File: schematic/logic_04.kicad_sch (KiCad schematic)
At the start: 4 parts, among them U418 74HC08, U421 74HC08, U423 74HC08, U425 74HC08

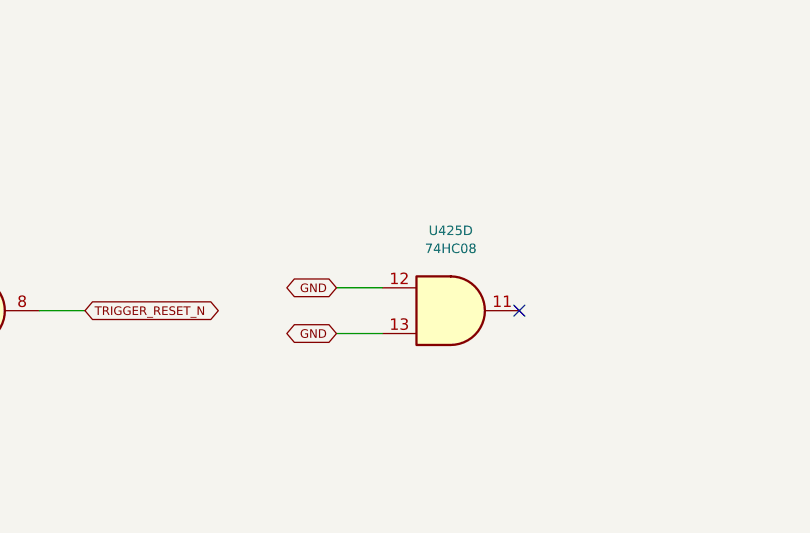
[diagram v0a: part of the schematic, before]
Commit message: add power supply, rail checks and parts list
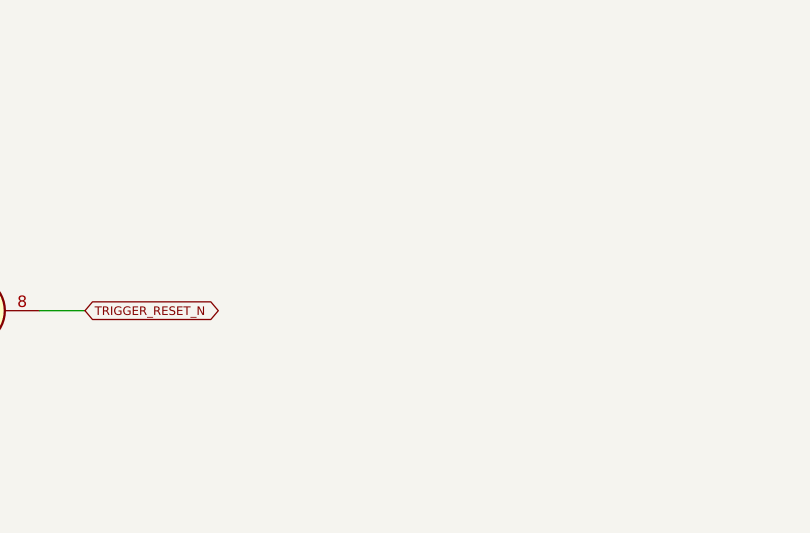
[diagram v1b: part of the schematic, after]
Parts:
- removed unit 4 of U425
- U418, U421, U423, U425: MPN (none) -> 74HC08D,653; Manufacturer (none) -> Nexperia; Supplier (none) -> LCSC
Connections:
- no-connect marks 1 -> 0
